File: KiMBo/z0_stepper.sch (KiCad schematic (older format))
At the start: 25 parts, among them U23 TMC2130

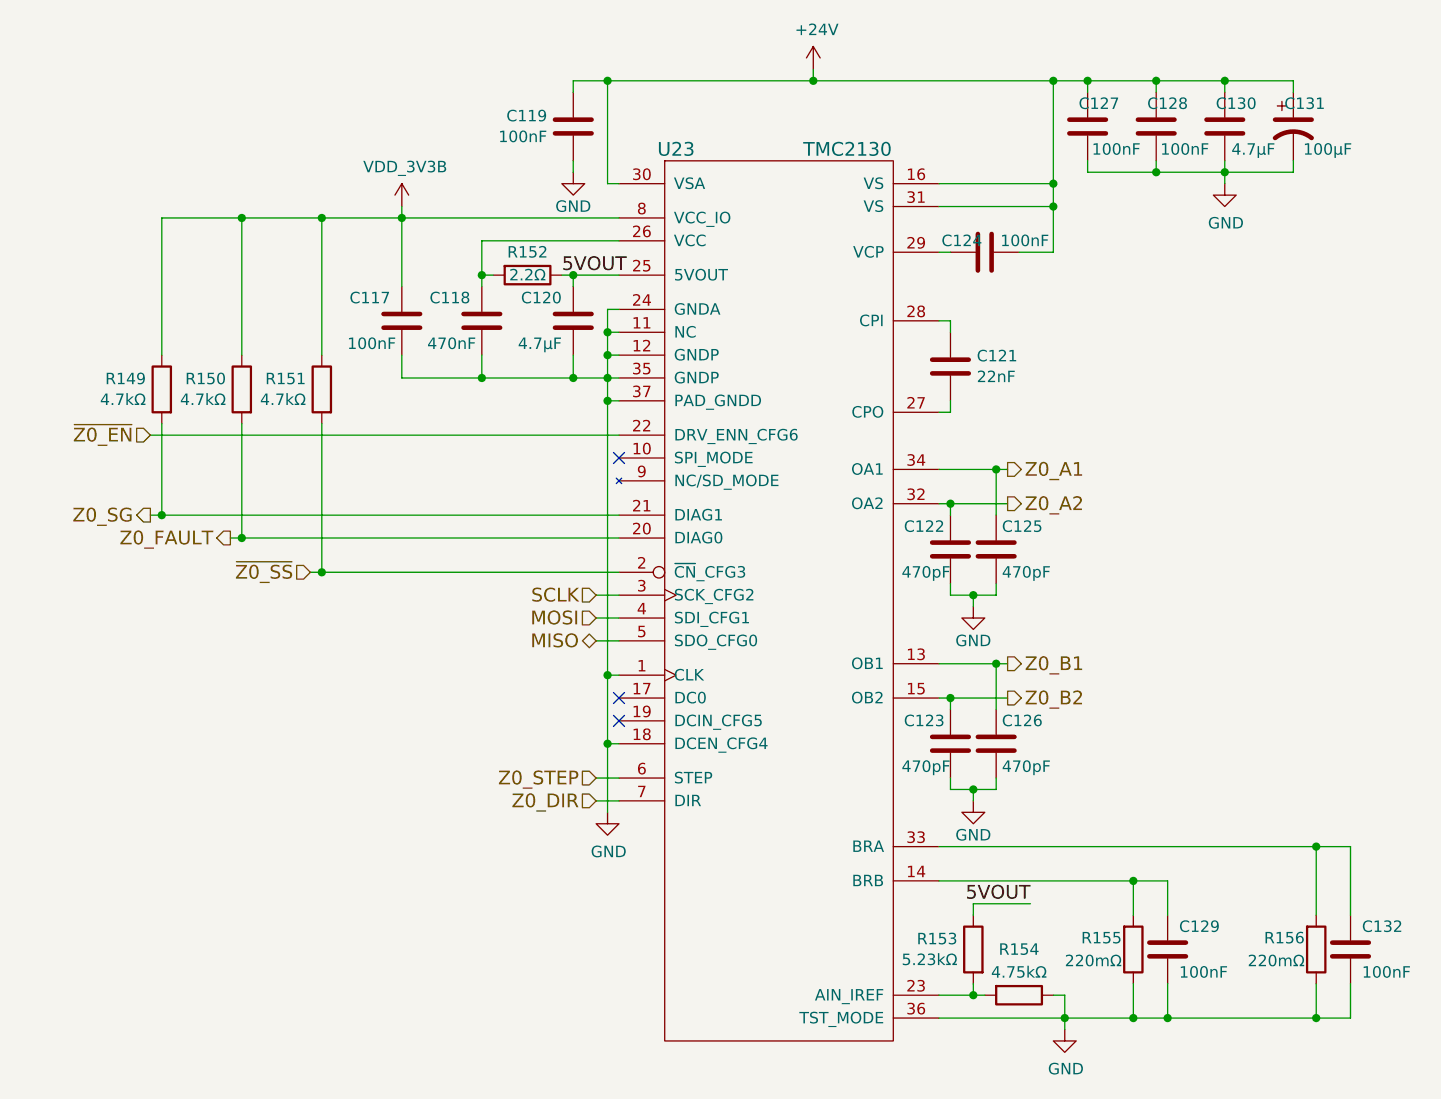
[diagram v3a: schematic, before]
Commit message: Entry of additional component values
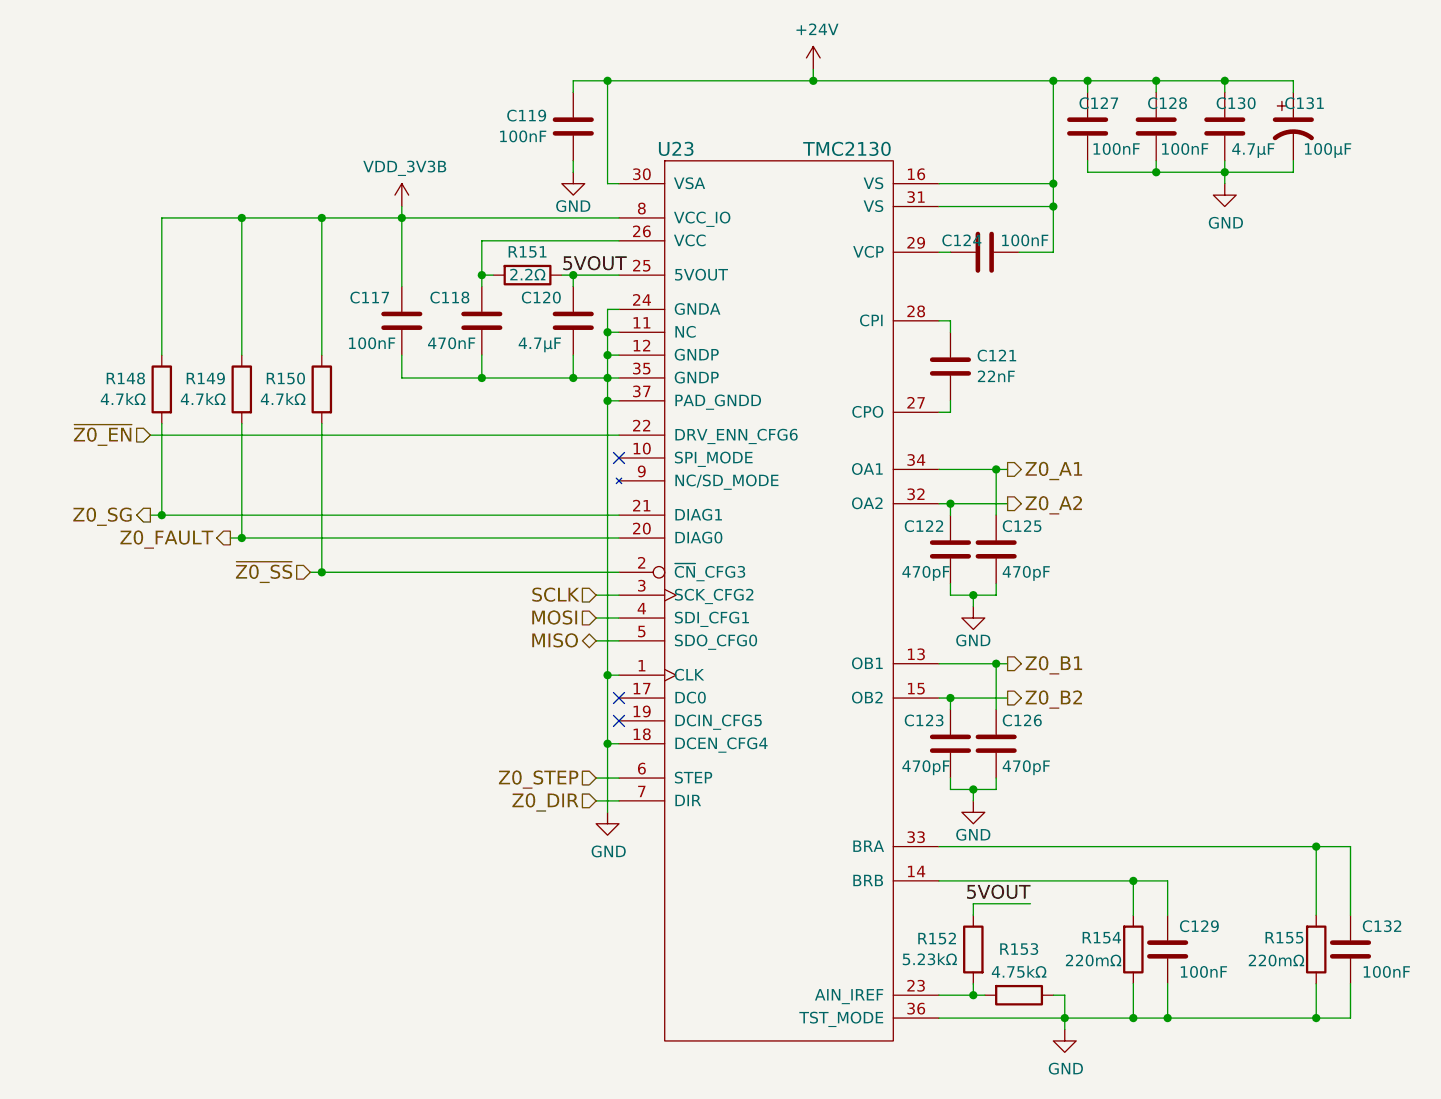
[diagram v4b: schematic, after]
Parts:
- renumbered R149 to R148, R150 to R149, R151 to R150, R152 to R151, R153 to R152, R154 to R153, R155 to R154, R156 to R155
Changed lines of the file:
@@
 $EndComp
 $Comp
-L GND #PWR0224
+L GND #PWR0225
 U 1 1 58C0C3E5
 P 7100 3350
-F 0 "#PWR0224" H 7100 3100 50  0001 C CNN
+F 0 "#PWR0225" H 7100 3100 50  0001 C CNN
 F 1 "GND" H 7100 3200 50  0000 C CNN
 F 2 "" H 7100 3350 50  0000 C CNN
@@
 $EndComp
 $Comp
-L GND #PWR0225
+L GND #PWR0226
 U 1 1 58C0C3F2
 P 9950 3400
-F 0 "#PWR0225" H 9950 3150 50  0001 C CNN
+F 0 "#PWR0226" H 9950 3150 50  0001 C CNN
 F 1 "GND" H 9955 3227 50  0000 C CNN
 F 2 "" H 9950 3400 50  0000 C CNN
@@
 $EndComp
 $Comp
-L +24V #PWR0226
+L +24V #PWR0227
 U 1 1 58C0C3F8
 P 8150 2900
-F 0 "#PWR0226" H 8150 2750 50  0001 C CNN
+F 0 "#PWR0227" H 8150 2750 50  0001 C CNN
 F 1 "+24V" H 8165 3073 50  0000 C CNN
 F 2 "" H 8150 2900 50  0000 C CNN
@@
 $EndComp
 $Comp
-L R R156
+L R R155
 U 1 1 58C0C405
 P 10350 6750
-F 0 "R156" H 10300 6700 50  0000 R CNN
+F 0 "R155" H 10300 6700 50  0000 R CNN
 F 1 "220mΩ" H 10300 6800 50  0000 R CNN
 F 2 "" V 10280 6750 50  0001 C CNN
@@
 $EndComp
 $Comp
-L R R155
+L R R154
 U 1 1 58C0C40C
 P 9550 6750
-F 0 "R155" H 9500 6700 50  0000 R CNN
+F 0 "R154" H 9500 6700 50  0000 R CNN
 F 1 "220mΩ" H 9500 6800 50  0000 R CNN
 F 2 "" V 9480 6750 50  0001 C CNN
@@
 $EndComp
 $Comp
-L GND #PWR0227
+L GND #PWR0228
 U 1 1 58C0C413
 P 9250 7100
-F 0 "#PWR0227" H 9250 6850 50  0001 C CNN
+F 0 "#PWR0228" H 9250 6850 50  0001 C CNN
 F 1 "GND" H 9255 6927 50  0000 C CNN
 F 2 "" H 9250 7100 50  0000 C CNN
@@
 NoConn ~ 7300 5650
 $Comp
-L R R152
+L R R151
 U 1 1 58C0C41A
 P 6900 3800
-F 0 "R152" V 6800 3800 50  0000 C CNN
+F 0 "R151" V 6800 3800 50  0000 C CNN
 F 1 "2.2Ω" V 6900 3800 50  0000 C CNN
 F 2 "" V 6830 3800 50  0001 C CNN
@@
 NoConn ~ 7300 5750
 $Comp
-L GND #PWR0228
+L GND #PWR0229
 U 1 1 58C0C436
 P 7250 6150
-F 0 "#PWR0228" H 7250 5900 50  0001 C CNN
+F 0 "#PWR0229" H 7250 5900 50  0001 C CNN
 F 1 "GND" H 7255 5977 50  0000 C CNN
 F 2 "" H 7250 6150 50  0000 C CNN
@@
 Z0_FAULT
 $Comp
-L R R150
+L R R149
 U 1 1 58C0C444
 P 5650 4300
-F 0 "R150" H 5719 4346 50  0000 L CNN
+F 0 "R149" H 5719 4346 50  0000 L CNN
 F 1 "4.7kΩ" H 5719 4255 50  0000 L CNN
 F 2 "" V 5580 4300 50  0001 C CNN
@@
 5VOUT
 $Comp
-L R R153
+L R R152
 U 1 1 58C0C456
 P 8850 6750
-F 0 "R153" H 8919 6796 50  0000 L CNN
+F 0 "R152" H 8919 6796 50  0000 L CNN
 F 1 "5.23kΩ" H 8919 6705 50  0000 L CNN
 F 2 "" V 8780 6750 50  0001 C CNN
@@
 5VOUT
 $Comp
-L R R154
+L R R153
 U 1 1 58C0C45E
 P 9050 6950
-F 0 "R154" V 8850 6950 50  0000 C CNN
+F 0 "R153" V 8850 6950 50  0000 C CNN
 F 1 "4.75kΩ" V 8950 6950 50  0000 C CNN
 F 2 "" V 8980 6950 50  0001 C CNN
@@
 $EndComp
 $Comp
-L R R151
+L R R150
 U 1 1 58C0C465
 P 6000 4300
-F 0 "R151" H 6069 4346 50  0000 L CNN
+F 0 "R150" H 6069 4346 50  0000 L CNN
 F 1 "4.7kΩ" H 6069 4255 50  0000 L CNN
 F 2 "" V 5930 4300 50  0001 C CNN
@@
 $EndComp
 $Comp
-L GND #PWR0229
+L GND #PWR0230
 U 1 1 58C0C47A
 P 8850 5250
-F 0 "#PWR0229" H 8850 5000 50  0001 C CNN
+F 0 "#PWR0230" H 8850 5000 50  0001 C CNN
 F 1 "GND" H 8850 5100 50  0000 C CNN
 F 2 "" H 8850 5250 50  0000 C CNN
@@
 $EndComp
 $Comp
-L GND #PWR0230
+L GND #PWR0231
 U 1 1 58C0C48E
 P 8850 6100
-F 0 "#PWR0230" H 8850 5850 50  0001 C CNN
+F 0 "#PWR0231" H 8850 5850 50  0001 C CNN
 F 1 "GND" H 8850 5950 50  0000 C CNN
 F 2 "" H 8850 6100 50  0000 C CNN
@@
 	8750 6050 8750 6000
 $Comp
-L R R149
+L R R148
 U 1 1 58C0C50F
 P 5300 4300
-F 0 "R149" H 5369 4346 50  0000 L CNN
+F 0 "R148" H 5369 4346 50  0000 L CNN
 F 1 "4.7kΩ" H 5369 4255 50  0000 L CNN
 F 2 "" V 5230 4300 50  0001 C CNN
@@
 	5300 3550 7300 3550
 $Comp
-L VDD_3V3B #PWR0231
+L VDD_3V3B #PWR0232
 U 1 1 5A313878
 P 6350 3500
-F 0 "#PWR0231" H 6350 3350 50  0001 C CNN
+F 0 "#PWR0232" H 6350 3350 50  0001 C CNN
 F 1 "VDD_3V3B" H 6365 3673 50  0000 C CNN
 F 2 "" H 6350 3500 50  0000 C CNN
